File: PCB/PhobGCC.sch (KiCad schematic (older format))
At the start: 43 parts, among them J1 Conn_01x06_Female, J2 Conn_01x04_Female, J3 Conn_01x01_Male, J4 Conn_01x01_Male, J6 10118194-0001LF, SW1 A, SW10 Dup, SW11 Dright, SW12 Ddown, SW2 B, SW3 X, SW4 Y, SW5 Start, SW6 L, SW7 R, SW8 1825027-5, SW9 Dleft, U1 Teensy3.2, U2 2x DRV5053CAQLPGM Hall Effect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

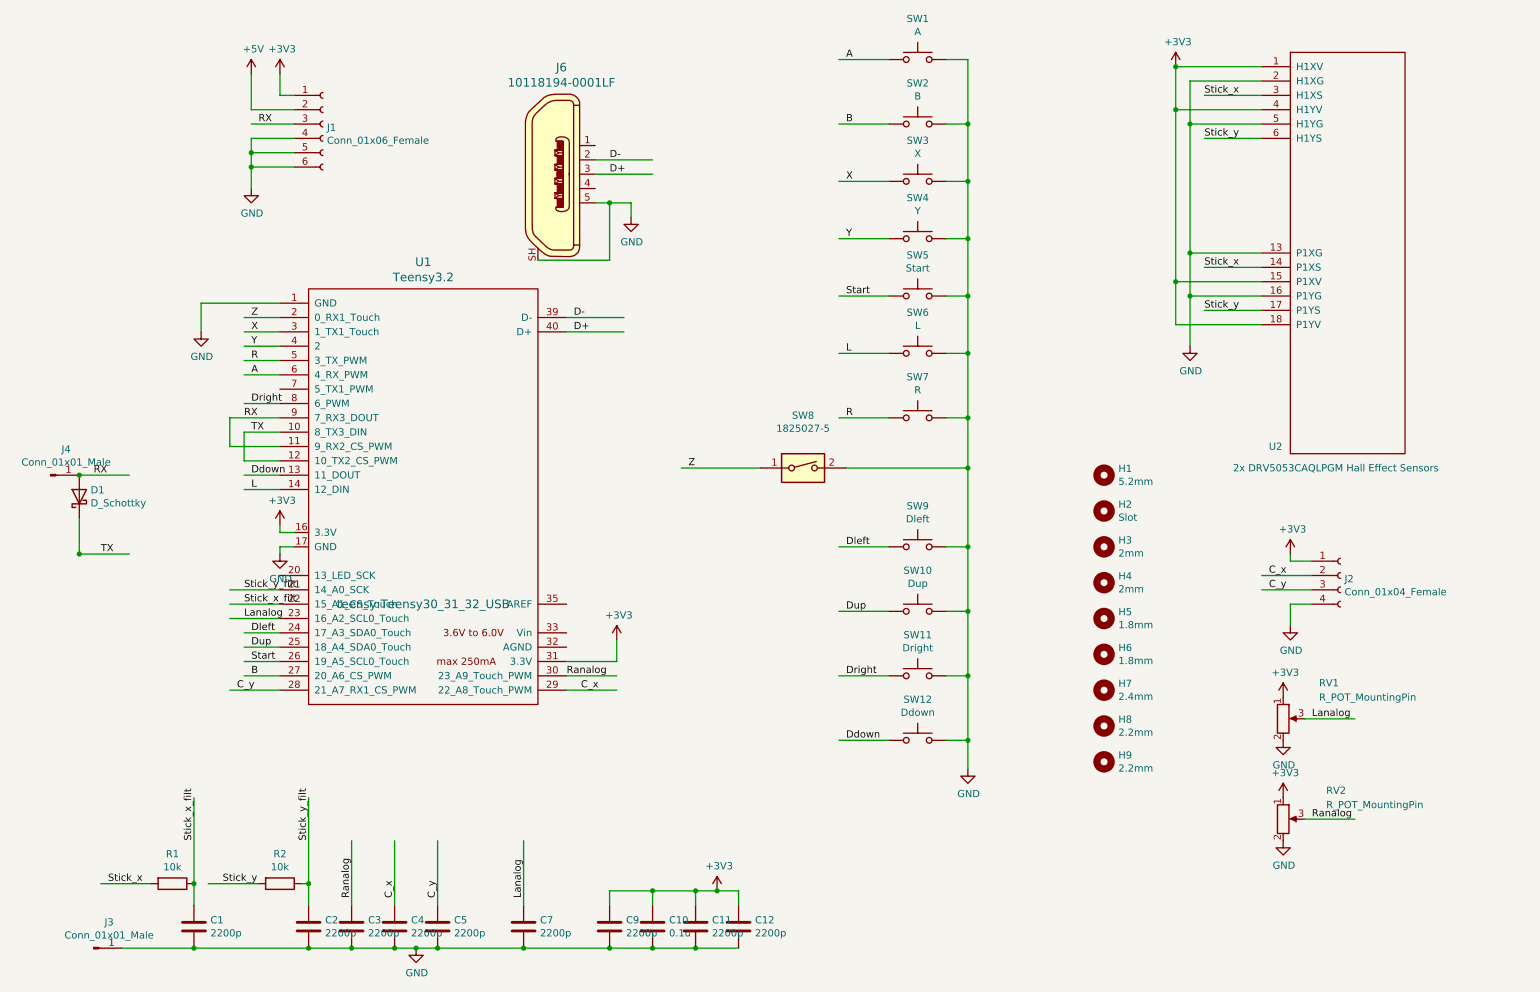
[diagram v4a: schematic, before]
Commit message: Changed the internal reference voltage check to update every loop. Changed the PCB to use a 2.5V regulator to power the hall effect sensors and pots as well as act as the ADC reference.
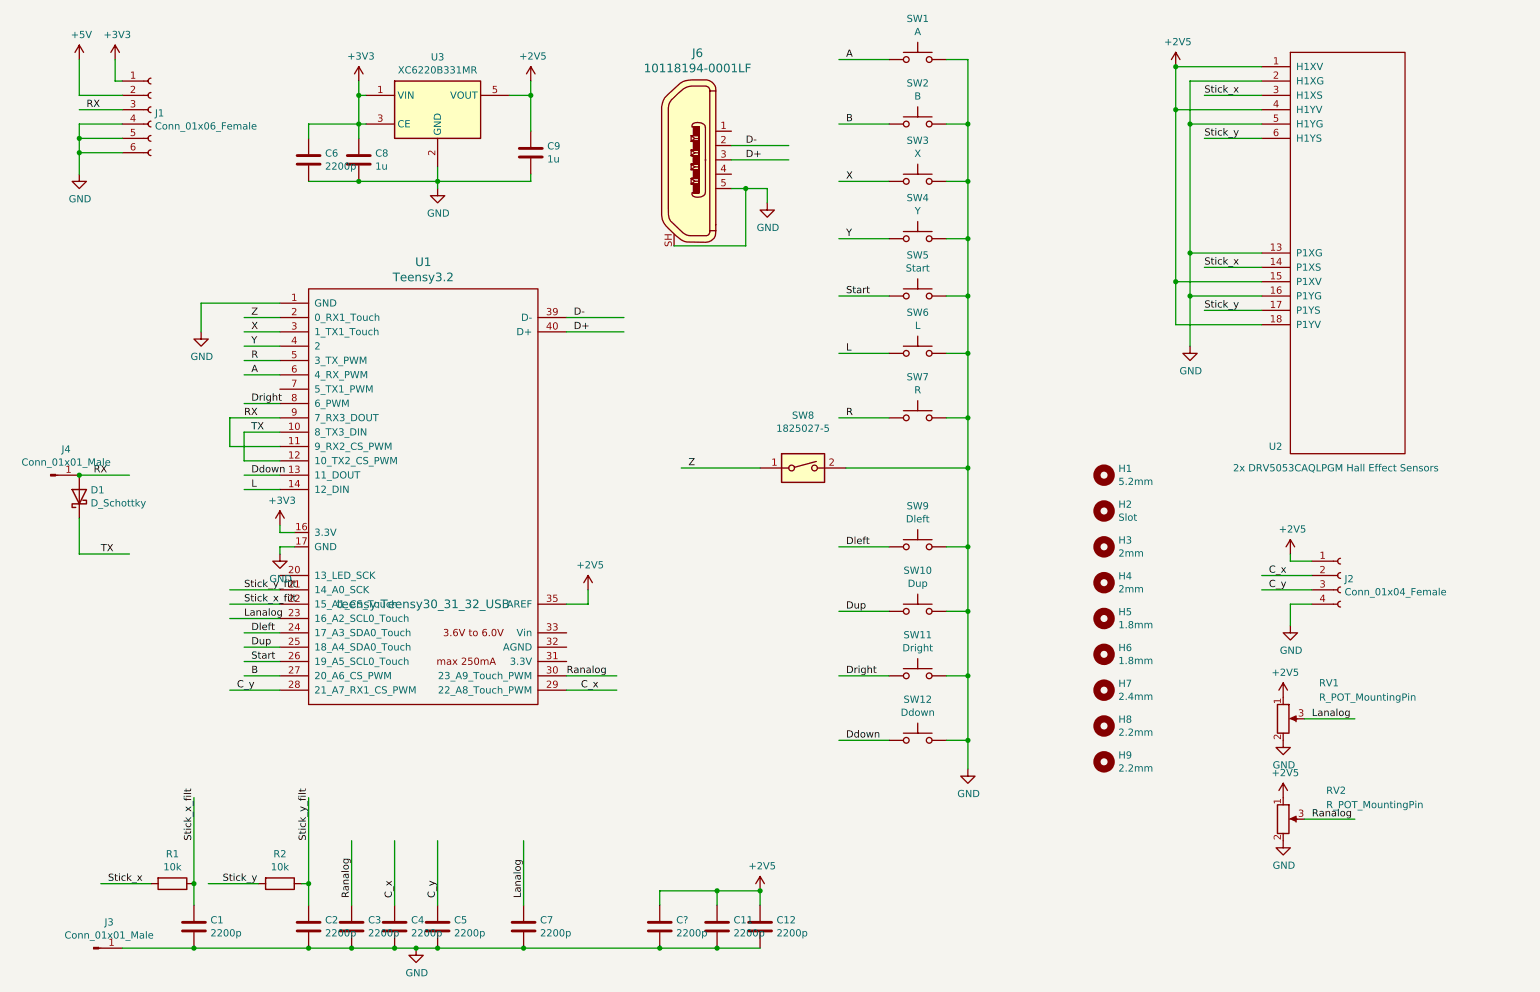
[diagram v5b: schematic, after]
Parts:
- removed C10: 0.1u, Capacitors_SMD:C_0603_HandSoldering, symbol Device:C
- added C6, C?: 2200p, Capacitors_SMD:C_0603_HandSoldering, symbol Device:C
- added C8: 1u, Capacitors_SMD:C_0603_HandSoldering, symbol Device:C
- added U3: XC6220B331MR, TO_SOT_Packages_SMD:SOT-23-5_HandSoldering, symbol Regulator_Linear:XC6220B331MR
- C9: value 2200p -> 1u
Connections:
- net labels added: +2V5
- wire segments 148 -> 160
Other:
- moved on the sheet: C11, C12, J1, J6

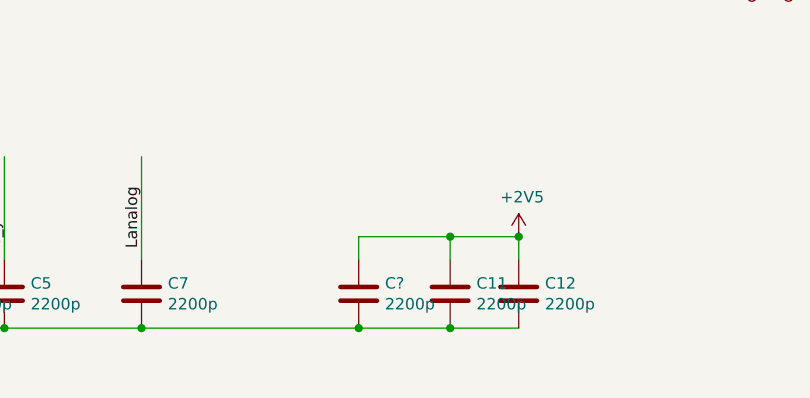
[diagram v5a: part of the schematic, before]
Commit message: Made it so that the serial frequency changes from 1000000 to 1250000 to respond to a command, this makes it appear to work with a wii u adapter.
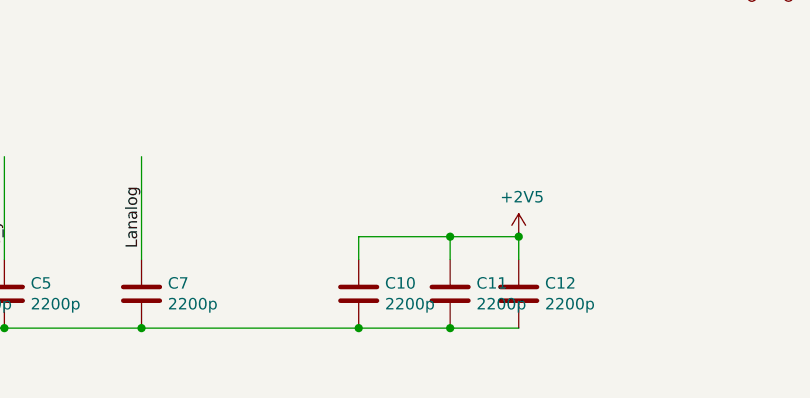
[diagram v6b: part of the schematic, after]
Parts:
- gave numbers to parts that had none: 1
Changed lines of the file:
@@
 	4350 4700 4350 4600
 $Comp
-L Device:C C?
+L Device:C C10
 U 1 1 61FB213E
 P 4850 6950
-F 0 "C?" H 4965 6996 50  0000 L CNN
+F 0 "C10" H 4965 6996 50  0000 L CNN
 F 1 "2200p" H 4965 6905 50  0000 L CNN
 F 2 "Capacitors_SMD:C_0603_HandSoldering" H 4888 6800 50  0001 C CNN
